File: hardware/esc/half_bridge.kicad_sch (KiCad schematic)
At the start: 4 parts, among them Q1 CSD17575Q3, Q2 CSD17575Q3

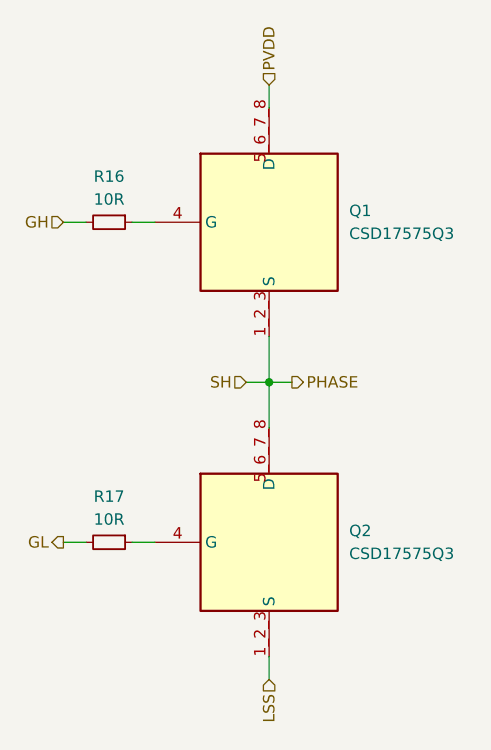
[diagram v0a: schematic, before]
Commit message: h: update BOM and FET for 5S
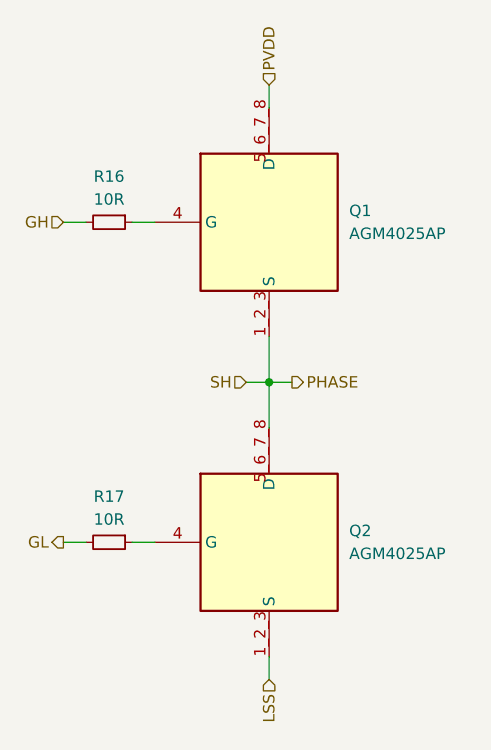
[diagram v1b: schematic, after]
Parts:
- Q1, Q2: value CSD17575Q3 -> AGM4025AP; LCSC# C529277 -> C42411651; MFR TI -> AGMSEMI; MPN CSD17575Q3 -> AGM4025AP
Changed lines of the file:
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@@
 			)
 		)
-		(property "Value" "CSD17575Q3"
+		(property "Value" "AGM4025AP"
 			(at 148.59 119.3799 0)
 			(show_name no)
@@
 			)
 		)
-		(property "Datasheet" "https://www.ti.com/lit/ds/symlink/csd17575q3.pdf"
+		(property "Datasheet" "https://www.lcsc.com/datasheet/C42411651.pdf"
 			(at 148.59 307.95 0)
 			(hide yes)
@@
 			)
 		)
-		(property "Description" "N-Channel MOSFET 30V 60A 2.8W"
+		(property "Description" "N-Channel MOSFET 40V"
 			(at 127 113.03 0)
 			(hide yes)
@@
 			)
 		)
-		(property "LCSC#" "C529277"
+		(property "LCSC#" "C42411651"
 			(at 127 113.03 0)
 			(hide yes)
@@
 			)
 		)
-		(property "MFR" "TI"
+		(property "MFR" "AGMSEMI"
 			(at 127 113.03 0)
 			(hide yes)
@@
 			)
 		)
-		(property "MPN" "CSD17575Q3"
+		(property "MPN" "AGM4025AP"
 			(at 127 113.03 0)
 			(hide yes)
@@
 			)
 		)
-		(property "Value" "CSD17575Q3"
+		(property "Value" "AGM4025AP"
 			(at 148.59 83.8199 0)
 			(show_name no)
@@
 			)
 		)
-		(property "Datasheet" "https://www.ti.com/lit/ds/symlink/csd17575q3.pdf"
+		(property "Datasheet" "https://www.lcsc.com/datasheet/C42411651.pdf"
 			(at 148.59 272.39 0)
 			(hide yes)
@@
 			)
 		)
-		(property "Description" "N-Channel MOSFET 30V 60A 2.8W"
+		(property "Description" "N-Channel MOSFET 30V"
 			(at 127 77.47 0)
 			(hide yes)
@@
 			)
 		)
-		(property "LCSC#" "C529277"
+		(property "LCSC#" "C42411651"
 			(at 127 77.47 0)
 			(hide yes)
@@
 			)
 		)
-		(property "MFR" "TI"
+		(property "MFR" "AGMSEMI"
 			(at 127 77.47 0)
 			(hide yes)
@@
 			)
 		)
-		(property "MPN" "CSD17575Q3"
+		(property "MPN" "AGM4025AP"
 			(at 127 77.47 0)
 			(hide yes)

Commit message: h: final changes before fab
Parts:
- R16, R17: value 10R -> 15R; LCSC# C138066 -> C138052; MPN RC0402FR-0710RL -> RC0402FR-0715RL
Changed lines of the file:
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@@
 			)
 		)
-		(property "Value" "10R"
+		(property "Value" "15R"
 			(at 121.92 115.57 90)
 			(show_name no)
@@
 			)
 		)
-		(property "LCSC#" "C138066"
+		(property "LCSC#" "C138052"
 			(at 121.92 118.11 90)
 			(hide yes)
@@
 			)
 		)
-		(property "MPN" "RC0402FR-0710RL"
+		(property "MPN" "RC0402FR-0715RL"
 			(at 121.92 118.11 90)
 			(hide yes)
@@
 			)
 		)
-		(property "Value" "10R"
+		(property "Value" "15R"
 			(at 121.92 80.01 90)
 			(show_name no)
@@
 			)
 		)
-		(property "Description" "0402 10R"
+		(property "Description" "0402 15R"
 			(at 121.92 82.55 0)
 			(hide yes)
@@
 			)
 		)
-		(property "LCSC#" "C138066"
+		(property "LCSC#" "C138052"
 			(at 121.92 82.55 90)
 			(hide yes)
@@
 			)
 		)
-		(property "MPN" "RC0402FR-0710RL"
+		(property "MPN" "RC0402FR-0715RL"
 			(at 121.92 82.55 90)
 			(hide yes)
